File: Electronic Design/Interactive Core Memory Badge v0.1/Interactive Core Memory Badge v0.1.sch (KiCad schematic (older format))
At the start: 7 parts, among them Q1 MMBT4403LT1G, Q2 MMBT4401LT1G

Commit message: Schematic Complete
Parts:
- added D3, D5: BAW56S, Package_TO_SOT_SMD:SOT-363_SC-70-6, symbol Diode:BAW56S
- added D4, D6: BAV70S, Package_TO_SOT_SMD:SOT-363_SC-70-6, symbol Diode:BAV70S
- added Q10, Q12, Q14, Q16, Q18, Q20, Q4, Q6, Q8: MMBT4401LT1G, Digikey:SOT-23-3, symbol Digikey-Transistors:MMBT4401LT1G
- added Q11, Q13, Q15, Q17, Q19, Q3, Q5, Q7, Q9: MMBT4403LT1G, Digikey:SOT-23-3, symbol Digikey-Transistors:MMBT4403LT1G
- added R10, R11, R12, R15, R22, R5: 6R8, Resistor_SMD:R_0805_2012Metric, symbol Device:R
- added R13, R14, R16, R17, R18, R19, R20, R21, R23, R24, R25, R26, R3, R4, R6, R7, R8, R9: 220, Resistor_SMD:R_0805_2012Metric, symbol Device:R
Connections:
- net XT4 is gone; now on net XT3-7: CM1.4 (XT3)
- net XT5 is gone; now on net XT2-6: CM1.3 (XT2)
- net XT6 is gone; now on net XT1-5: CM1.2 (XT1)
- net XT7 is gone; now on net XT0-4: CM1.1 (XT0)
- net XB0: now also CM1.24 (XB0), D1.1 (K), D2.1 (A); no longer CM1.17 (XB7)
- net XB1: now also CM1.23 (XB1), D1.2 (K), D2.2 (A); no longer CM1.18 (XB6)
- net XB2: now also CM1.22 (XB2), D1.4 (K), D2.4 (A); no longer CM1.19 (XB5)
- net XB3: now also CM1.21 (XB3), D1.5 (K), D2.5 (A); no longer CM1.20 (XB4)
- net XB4: now also CM1.20 (XB4), D3.1 (K), D4.1 (A); no longer CM1.21 (XB3), D1.5 (K), D2.5 (A)
- net XB5: now also CM1.19 (XB5), D3.2 (K), D4.2 (A); no longer CM1.22 (XB2), D1.4 (K), D2.4 (A)
- net XB6: now also CM1.18 (XB6), D3.4 (K), D4.4 (A); no longer CM1.23 (XB1), D1.2 (K), D2.2 (A)
- net XB7: now also CM1.17 (XB7), D3.5 (K), D4.5 (A); no longer CM1.24 (XB0), D1.1 (K), D2.1 (A)
- net YL1: now reaches CM1.10 (YL1)
- net YL1: now also D5.1 (K), D6.2 (A)
- net YL2: now reaches CM1.11 (YL2)
- net YL2: now also D5.5 (K), D6.4 (A)
- net YL3: now reaches CM1.12 (YL3)
- net YL3: now also D5.2 (K), D6.5 (A)
- net YL4: now reaches CM1.13 (YL4)
- net YL4: now also CM1.15 (YL6), R11.1
- net YL5: now reaches CM1.14 (YL5)
- net YL5: now also CM1.16 (YL7), R12.1
- net SENSE1: now reaches CM1.33 (S1)
- net SENSE2: now reaches CM1.34 (S2)
- net YL0: now reaches CM1.9 (YL0)
- net YL0: now also D5.4 (K), D6.1 (A)
- net +BATT renamed VMEM
- net VMEM: now also Q11.2 (E), Q13.2 (E), Q15.2 (E), Q17.2 (E), Q19.2 (E), Q3.2 (E), Q5.2 (E), Q7.2 (E), Q9.2 (E)
- net -BATT renamed GNDPWR
- net GNDPWR: now also Q10.2 (E), Q12.2 (E), Q14.2 (E), Q16.2 (E), Q18.2 (E), Q20.2 (E), Q4.2 (E), Q6.2 (E), Q8.2 (E)
- net XT0 renamed XT3-7
- net XT3-7: now also R22.1
- net XT1 renamed XT2-6
- net XT2-6: now also R15.1
- net XT2 renamed XT1-5
- net XT1-5: now also R10.1
- net XT3 renamed XT0-4
- net XT0-4: now also R5.2
- new net: Q4.1 (B), R4.1
- new net: Q3.1 (B), R3.1
- new net: Q3.3 (C), Q4.3 (C), R5.1
- new net: D5.3 (A), D5.6 (A), Q17.3 (C)
- new net: Q17.1 (B), R23.1
- new net: Q18.1 (B), R24.1
- new net: D6.6 (K), Q18.3 (C)
- new net: D3.3 (A), D3.3 (A), D3.6 (A), D3.6 (A), Q5.3 (C)
- new net: Q5.1 (B), R6.1
- new net: Q6.1 (B), R7.1
- new net: D4.3 (K), D4.6 (K), Q6.3 (C)
- new net: D5.3 (A), D5.6 (A), Q19.3 (C)
- new net: Q19.1 (B), R25.1
- new net: Q20.1 (B), R26.1
- new net: D6.3 (K), Q20.3 (C)
- new net: Q7.1 (B), R8.1
- new net: Q7.3 (C), Q8.3 (C), R10.2
- new net: Q8.1 (B), R9.1
- new net: Q13.1 (B), R13.1
- new net: Q13.3 (C), Q14.3 (C), R15.2
- new net: Q14.1 (B), R14.1
- new net: Q15.1 (B), R20.1
- new net: Q15.3 (C), Q16.3 (C), R22.2
- new net: Q16.1 (B), R21.1
- new net: Q9.1 (B), R18.1
- new net: Q10.3 (C), Q9.3 (C), R11.2
- new net: Q10.1 (B), R19.1
- new net: Q11.1 (B), R16.1
- new net: Q11.3 (C), Q12.3 (C), R12.2
- new net: Q12.1 (B), R17.1
- new net Q10N: R17.2
- new net Q10P: R16.2
- new net Q2N: R7.2
- new net Q2P: R6.2
- new net Q3N: R4.2
- new net Q3P: R3.2
- new net Q4N: R9.2
- new net Q4P: R8.2
- new net Q5N: R14.2
- new net Q5P: R13.2
- new net Q6N: R21.2
- new net Q6P: R20.2
- new net Q7N: R24.2
- new net Q7P: R23.2
- new net Q8N: R26.2
- new net Q8P: R25.2
- new net Q9N: R19.2
- new net Q9P: R18.2
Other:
- moved on the sheet: CM1

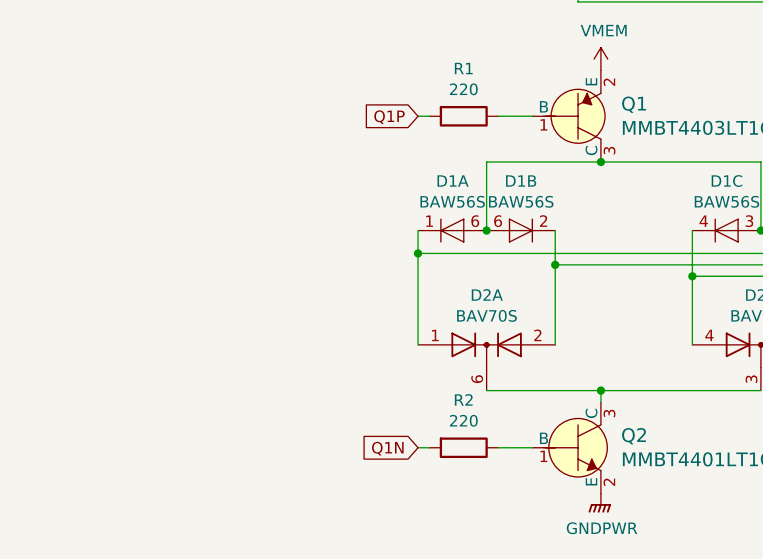
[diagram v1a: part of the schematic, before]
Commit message: Layout 75% complete for V0.1
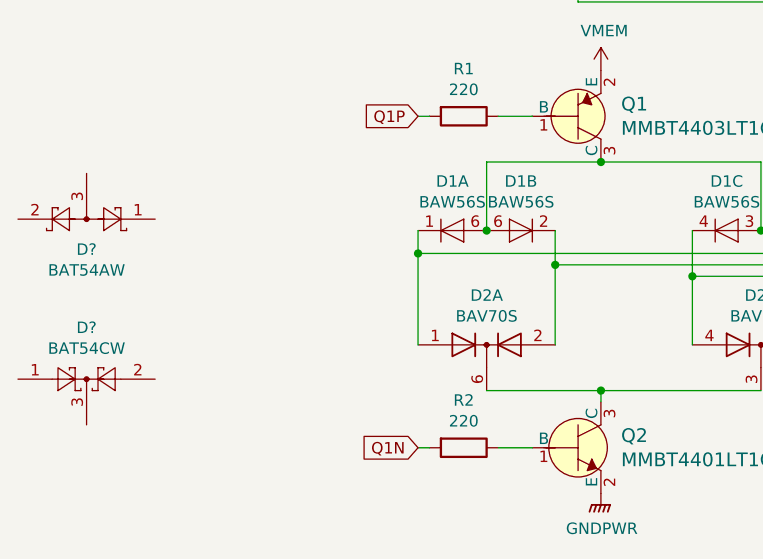
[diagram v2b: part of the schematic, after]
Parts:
- added D?: BAT54AW, Package_TO_SOT_SMD:SOT-323_SC-70, symbol Diode:BAT54AW
- added D?: BAT54CW, Package_TO_SOT_SMD:SOT-323_SC-70, symbol Diode:BAT54CW

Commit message: Prototype release V0.1
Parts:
- removed D1, D3, D5: BAW56S, Package_TO_SOT_SMD:SOT-363_SC-70-6, symbol Diode:BAW56S
- removed D2, D4, D6: BAV70S, Package_TO_SOT_SMD:SOT-363_SC-70-6, symbol Diode:BAV70S
- added D10, D12, D4, D6, D8: BAT54CW, Package_TO_SOT_SMD:SOT-323_SC-70, symbol Diode:BAT54CW
- added D11, D3, D5, D7, D9: BAT54AW, Package_TO_SOT_SMD:SOT-323_SC-70, symbol Diode:BAT54AW
- gave numbers to parts that had none: 2
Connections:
- net XB0: now also D1.2, D2.1
- net XB1: now also D1.1, D2.2
- net XB2: now also D3.2, D4.1
- net XB3: now also D3.1, D4.2
- net XB4: now also D5.2, D6.1
- net XB5: now also D5.1, D6.2
- net XB6: now also D7.2, D8.1
- net XB7: now also D7.1, D8.2
- net YL0: now also D10.2, D9.1
- net YL1: now also D10.1, D9.2
- net YL2: now also D11.1, D12.2
- net YL3: now also D11.2, D12.1
- net at Q1.3 (C): now also D1.3, D3.3
- net at Q2.3 (C): now also D2.3, D4.3
- net at Q17.3 (C): now also D9.3
- net at Q18.3 (C): now also D10.3
- net at Q5.3 (C): now also D5.3, D7.3
- net at Q6.3 (C): now also D6.3, D8.3
- net at Q19.3 (C): now also D11.3
- net at Q20.3 (C): now also D12.3
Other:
- moved on the sheet: D1, D2
